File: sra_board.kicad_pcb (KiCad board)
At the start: 2 copper layers, 90 x 86.8 mm, 164 parts, among them J1 Conn_01x14_Pin, J10 Conn_01x03_Pin, J11 Conn_01x03_Pin, J12 Conn_01x03_Pin, J13 MPU0650, J14 LSA, J15 OLED, J16 Conn_01x03_Pin, J17 Conn_01x03_Pin, J18 Conn_01x03_Pin, J3 Conn_01x08_Pin, J4 Conn_01x14_Pin, J5 USB_C_Receptacle_USB2.0_16P, J6 B2B-XH-A_LF__SN_, J7 B2B-XH-A_LF__SN_, J8 B2B-XH-A_LF__SN_, J9 Conn_01x03_Pin, Q1 SS8050, Q2 SS8050, Q3 AO3400A, Q4 AO3401A, Q5 AO3401A, Q6 AO3401A, Q7 AO3401A, SW1 SW_0, SW2 SW_EN, SW3 Switch, SW4 Switch, SW5 SW_Wuerth_450301014042, SW6 SW_Wuerth_450301014042, U1 MAX7219CWG_T, U2 CH340C, U3 TB6612FNG H-bridge Motor Driv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, U5 CN3303, U6 TPS562202, U7 ME6211C33M5, U8 ESP32-WROOM-32E

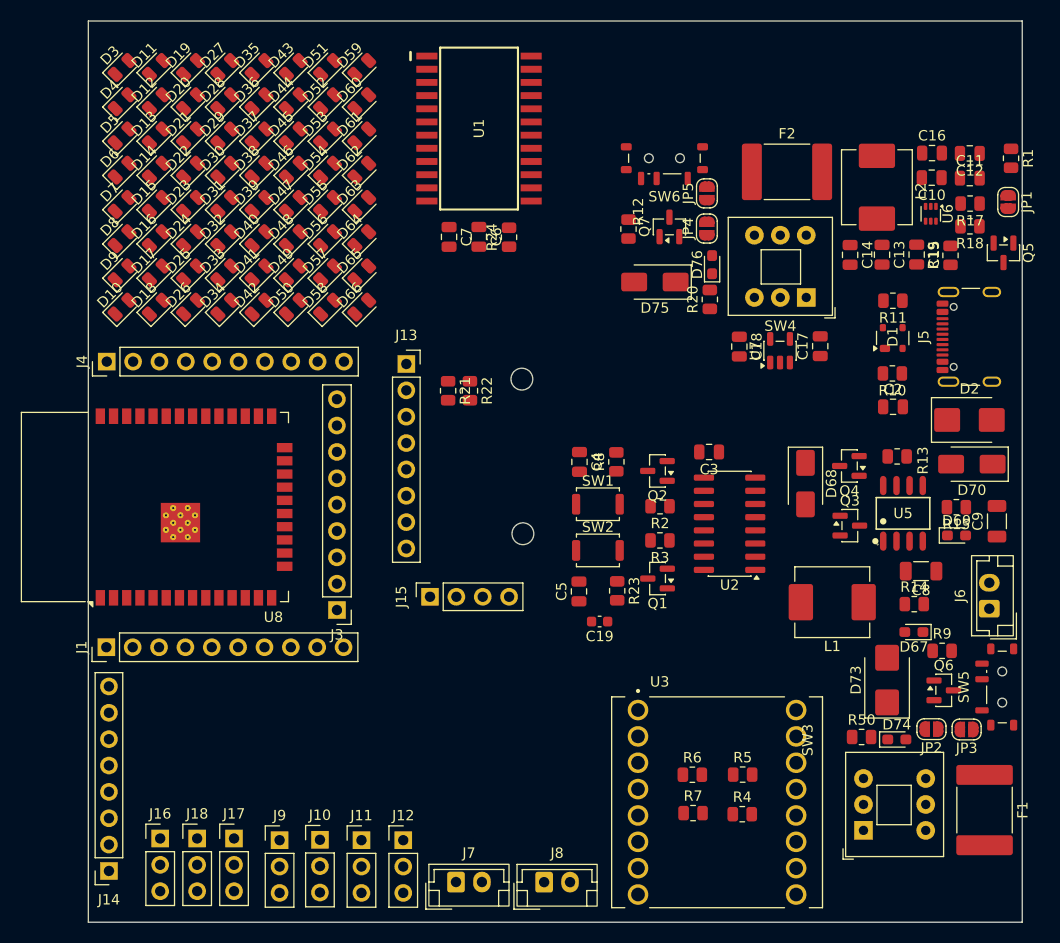
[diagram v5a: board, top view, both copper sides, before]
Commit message: Placement first draft along with 3D files
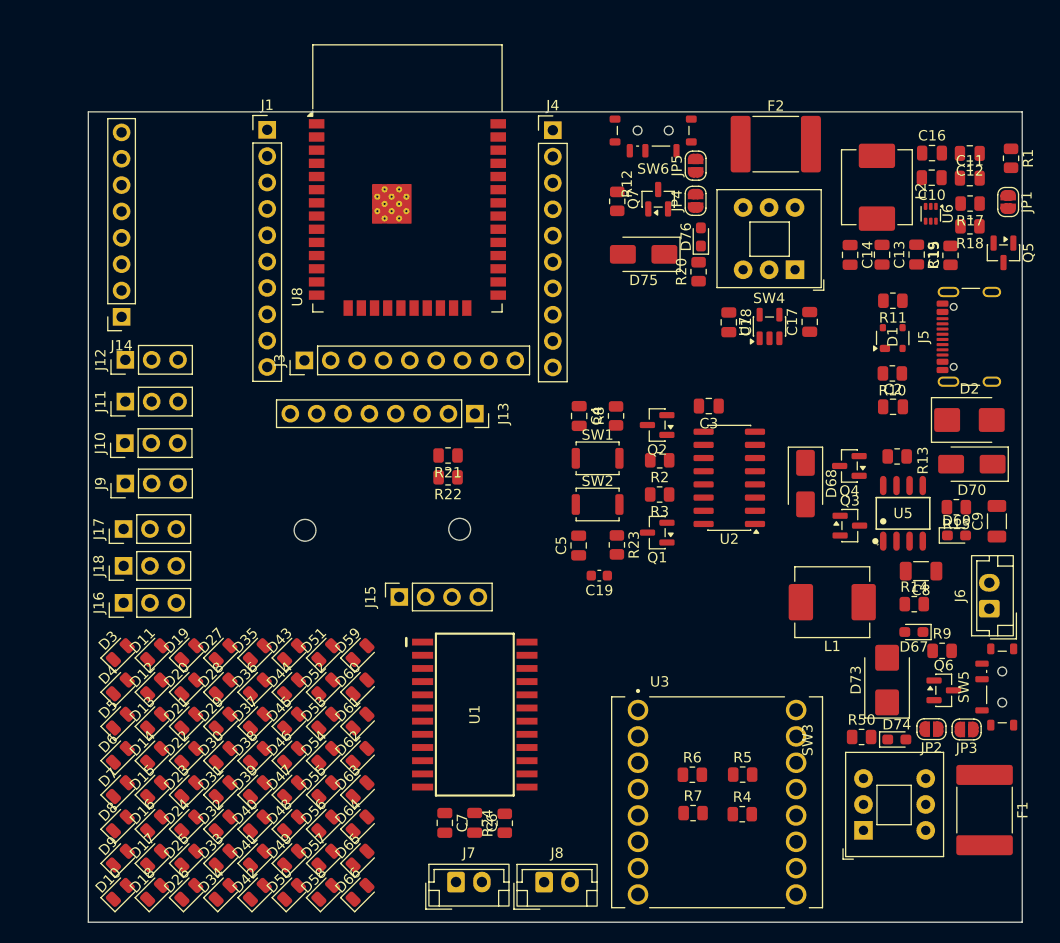
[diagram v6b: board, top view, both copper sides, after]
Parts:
- moved U1 56.5 mm to (170.5, 81.9)
- moved C6 56.5 mm to (170.4, 92.3)
- moved C7 56.5 mm to (167.6, 92.3)
- moved R24 56.5 mm to (173.3, 92.4)
- moved D11 56.4 mm to (139.6, 75.9)
- moved D15 56.4 mm to (139.6, 89.1)
- moved D16 56.4 mm to (139.6, 92.4)
- moved D17 56.4 mm to (139.6, 95.7)
- moved D19 56.4 mm to (142.9, 75.9)
- moved D23 56.4 mm to (142.9, 89.1)
- moved D24 56.4 mm to (142.9, 92.4)
- moved D25 56.4 mm to (142.9, 95.7)
- moved D27 56.4 mm to (146.2, 75.9)
- moved D3 56.4 mm to (136.3, 75.9)
- moved D31 56.4 mm to (146.2, 89.1)
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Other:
- board size 90 x 86.8 mm -> 90 x 78.1 mm

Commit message: Finishing the routing
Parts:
- added ?: , , F.Cu at (200.8, 136.2)
- added ?: , , F.Cu at (118.0, 136.2)
- added H1: MountingHole, MountingHole:MountingHole_3.2mm_M3, F.Cu at (200.7, 53.5)
- added H4: MountingHole, MountingHole:MountingHole_3.2mm_M3, F.Cu at (118.0, 53.5)
- C19: footprint Capacitor_SMD:C_0603_1608Metric -> Capacitor_SMD:C_0805_2012Metric
- J14: footprint Connector_PinSocket_2.54mm:PinSocket_1x08_P2.54mm_Vertical -> Connector_PinSocket_2.54mm:PinSocket_1x07_P2.54mm_Vertical
- J3: footprint Connector_PinHeader_2.54mm:PinHeader_1x09_P2.54mm_Vertical -> Connector_PinHeader_2.54mm:PinHeader_1x10_P2.54mm_Vertical
- JP1, JP2, JP3, JP4, JP5: footprint Jumper:SolderJumper-2_P1.3mm_Open_RoundedPad1.0x1.5mm -> Connector_PinHeader_2.54mm:PinHeader_1x02_P2.54mm_Vertical
- R13: footprint Resistor_SMD:R_0805_2012Metric -> Resistor_SMD:R_1206_3216Metric
- moved C2 93.3 mm to (149.4, 122.4), turned to -90 degrees
- moved R8 92.6 mm to (129.4, 127.9), turned to -90 degrees
- moved C4 92.6 mm to (125.8, 127.9), turned to 90 degrees
- moved J1 91.4 mm to (116.2, 110.3), turned to 90 degrees
- moved Q2 89.4 mm to (133.5, 124.9)
- moved J14 88.1 mm to (117.0, 129.5)
- moved SW1 85.9 mm to (127.6, 123.4)
- moved J12 85.1 mm to (127.0, 132.2), turned to 0 degrees
- moved J4 84.1 mm to (116.2, 82.7), turned to 90 degrees
- moved J11 81.7 mm to (123.1, 132.3), turned to 0 degrees
- moved R3 81.5 mm to (137.8, 124.8), turned to -90 degrees
- moved U2 80.2 mm to (143.7, 120.7)
- moved SW2 79.1 mm to (127.6, 118.7)
- moved C3 79.0 mm to (143.8, 114.0), turned to 0 degrees
- moved R2 78.6 mm to (137.9, 117.7), turned to 90 degrees
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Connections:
- net /7V4_Switch renamed /12V_Switch
- net /7v4 renamed /12V
- J3 pad 6: /2 -> /15
- J3 pad 7: /16 -> /2
- J3 pad 8: /4 -> /16
- J3 pad 9: /0 -> /4
- J4 pad 2: /Din -> /23
- J4 pad 8: /CLK -> /18
- J4 pad 9: /CS -> /5
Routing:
- net /3V3: track 0.00 -> 256.3 mm, vias 0 -> 4
- net /5V_P: track 0.00 -> 218.7 mm, vias 0 -> 1
- net /5V_P_USB: track 0.00 -> 124.1 mm
- net /12V: track 0.00 -> 114.4 mm, vias 0 -> 2
- net /0: track 0.00 -> 93.6 mm, vias 0 -> 1
- net /22: track 0.00 -> 86.9 mm
- net /19: track 0.00 -> 75.5 mm, vias 0 -> 1
- net /D-: track 0.00 -> 68.4 mm
- net /D+: track 0.00 -> 67.0 mm, vias 0 -> 2
- net /21: track 0.00 -> 63.3 mm
- net /C1: track 0.00 -> 63.1 mm, vias 0 -> 2
- net /C2: track 0.00 -> 63.1 mm, vias 0 -> 5
- net /C3: track 0.00 -> 63.0 mm, vias 0 -> 5
- net /TXD: track 0.00 -> 61.9 mm, vias 0 -> 2
- net /R2: track 0.00 -> 61.8 mm
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- added copper zone on B.Cu, net GND
- added copper zone on F.Cu, net GND
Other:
- board size 90 x 78.1 mm -> 90 x 89.5 mm
